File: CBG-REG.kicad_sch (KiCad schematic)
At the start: 36 parts, among them J1 Conn_01x09_Socket, J2 Conn_01x09_Socket, U1 AD8560ACP-REEL7, U2 AD8560ACP-REEL7, U4 74LVC2G04

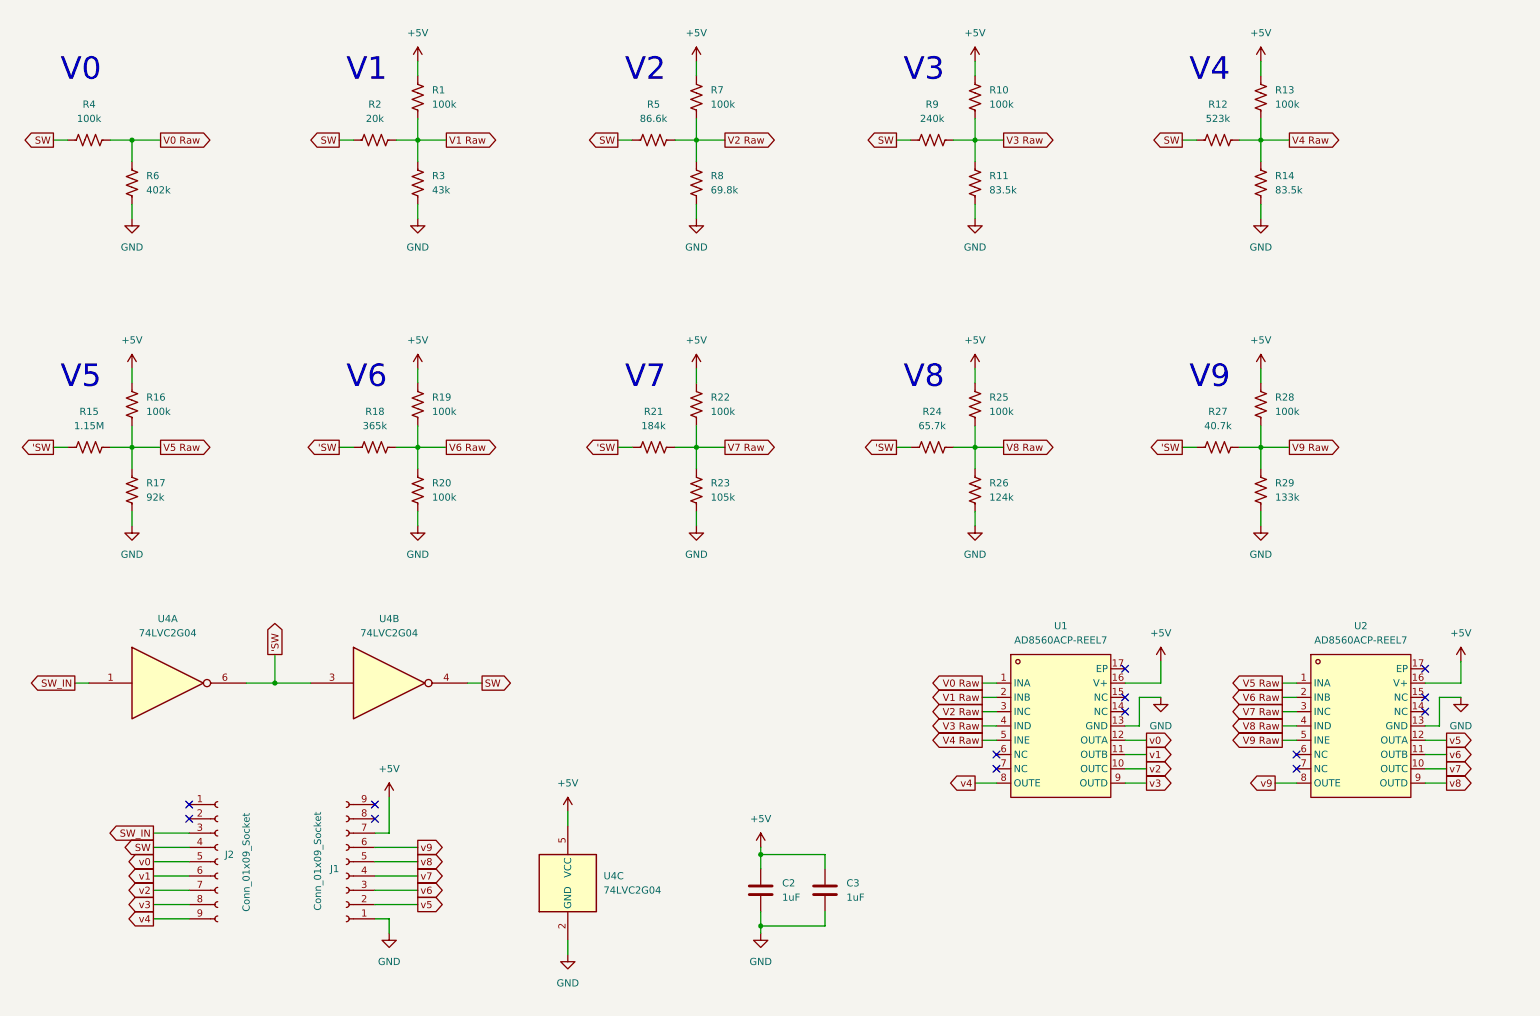
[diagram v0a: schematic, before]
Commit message: fix: Update resistor values to those in stock at JLCPCB
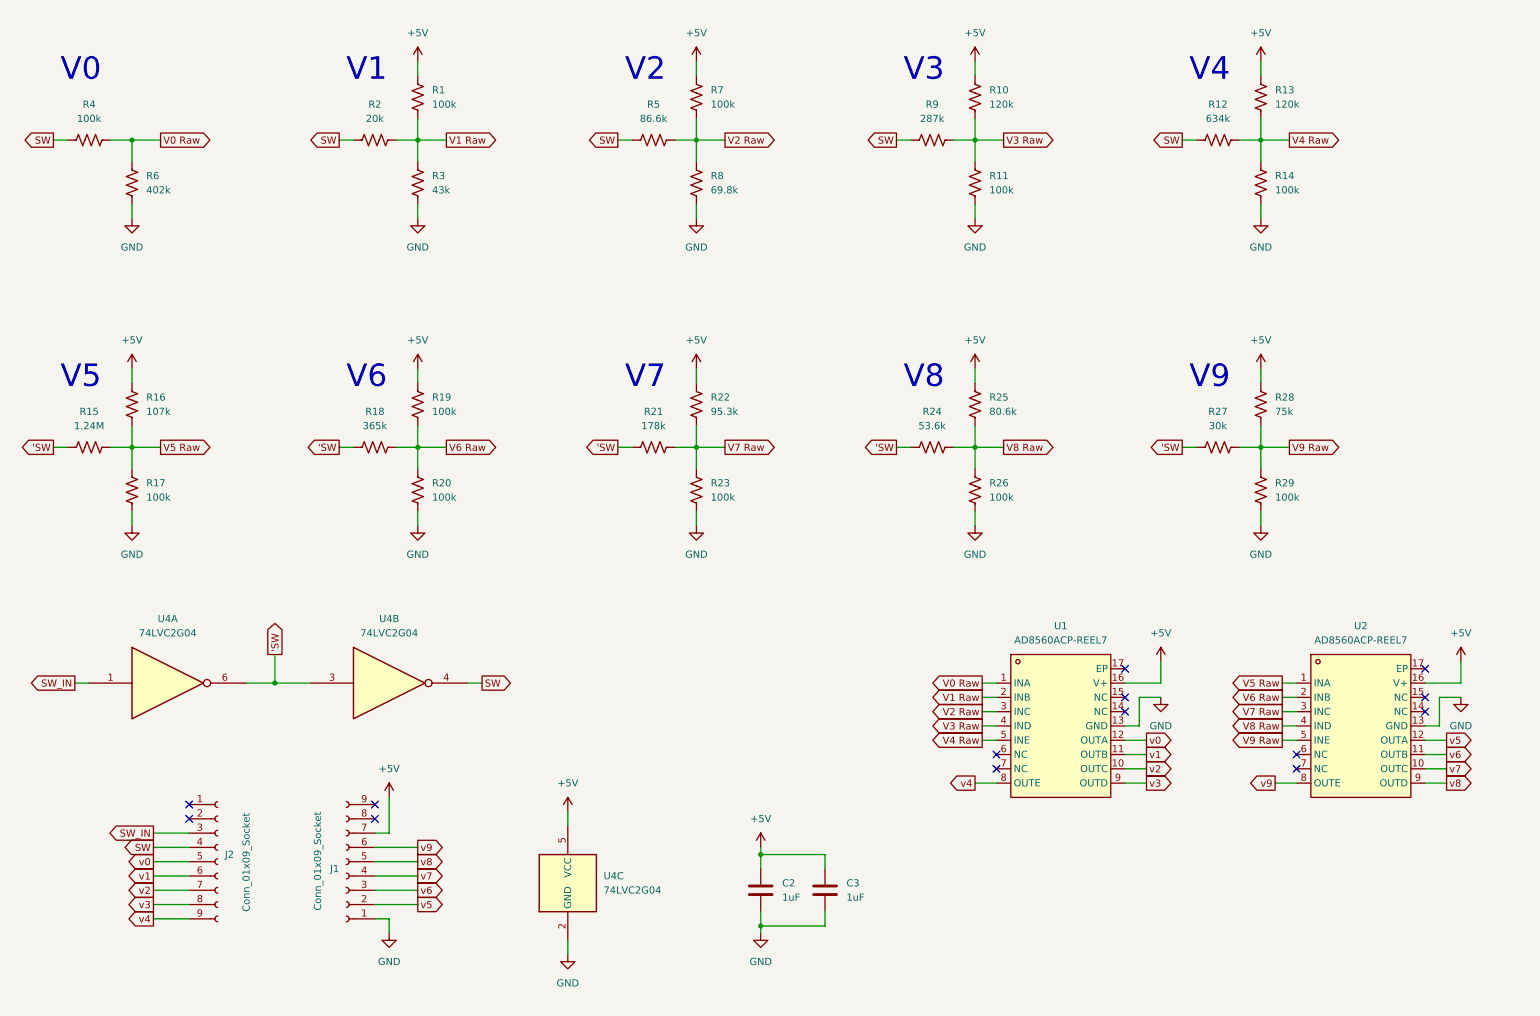
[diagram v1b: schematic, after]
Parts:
- R10, R13: value 100k -> 120k; LCSC C414506 -> C325641
- R11, R14: value 83.5k -> 100k; LCSC C3915798 -> C414506
- R12: value 523k -> 634k; LCSC C5126197 -> C321970
- R15: value 1.15M -> 1.24M; LCSC C2100176 -> C367719
- R16: value 100k -> 107k; LCSC C414506 -> C103221
- R17: value 92k -> 100k; LCSC C4024522 -> C414506
- R21: value 184k -> 178k; LCSC C2505474 -> C103349
- R22: value 100k -> 95.3k; LCSC C414506 -> C912224
- R23: value 105k -> 100k; LCSC C100713 -> C414506
- R24: value 65.7k -> 53.6k; LCSC C2498169 -> C103706
- R25: value 100k -> 80.6k; LCSC C414506 -> C2933260
- R26: value 124k -> 100k; LCSC C2889164 -> C414506
- R27: value 40.7k -> 30k; LCSC C2495443 -> C667692
- R28: value 100k -> 75k; LCSC C414506 -> C881187
- R29: value 133k -> 100k; LCSC C317180 -> C414506
- R9: value 240k -> 287k; LCSC C881412 -> C13174
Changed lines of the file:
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@@
       (effects (font (size 1.27 1.27)) (justify left))
     )
-    (property "Value" "100k" (at 187.96 34.29 0)
+    (property "Value" "120k" (at 187.96 34.29 0)
       (effects (font (size 1.27 1.27)) (justify left))
     )
@@
       (effects (font (size 1.27 1.27)) hide)
     )
-    (property "LCSC" "C414506" (at 185.42 33.02 0)
+    (property "LCSC" "C325641" (at 185.42 33.02 0)
       (effects (font (size 1.27 1.27)) hide)
     )
@@
       (effects (font (size 1.27 1.27)) (justify left))
     )
-    (property "Value" "105k" (at 138.43 104.14 0)
+    (property "Value" "100k" (at 138.43 104.14 0)
       (effects (font (size 1.27 1.27)) (justify left))
     )
@@
       (effects (font (size 1.27 1.27)) hide)
     )
-    (property "LCSC" "C100713" (at 135.89 102.87 0)
+    (property "LCSC" "C414506" (at 135.89 102.87 0)
       (effects (font (size 1.27 1.27)) hide)
     )
@@
       (effects (font (size 1.27 1.27)) (justify left))
     )
-    (property "Value" "100k" (at 238.76 88.9 0)
+    (property "Value" "75k" (at 238.76 88.9 0)
       (effects (font (size 1.27 1.27)) (justify left))
     )
@@
       (effects (font (size 1.27 1.27)) hide)
     )
-    (property "LCSC" "C414506" (at 236.22 87.63 0)
+    (property "LCSC" "C881187" (at 236.22 87.63 0)
       (effects (font (size 1.27 1.27)) hide)
     )
@@
       (effects (font (size 1.27 1.27)) (justify left))
     )
-    (property "Value" "83.5k" (at 238.76 49.53 0)
+    (property "Value" "100k" (at 238.76 49.53 0)
       (effects (font (size 1.27 1.27)) (justify left))
     )
@@
       (effects (font (size 1.27 1.27)) hide)
     )
-    (property "LCSC" "C3915798" (at 236.22 48.26 0)
+    (property "LCSC" "C414506" (at 236.22 48.26 0)
       (effects (font (size 1.27 1.27)) hide)
     )
@@
       (effects (font (size 1.27 1.27)) (justify left))
     )
-    (property "Value" "83.5k" (at 187.96 49.53 0)
+    (property "Value" "100k" (at 187.96 49.53 0)
       (effects (font (size 1.27 1.27)) (justify left))
     )
@@
       (effects (font (size 1.27 1.27)) hide)
     )
-    (property "LCSC" "C3915798" (at 185.42 48.26 0)
+    (property "LCSC" "C414506" (at 185.42 48.26 0)
       (effects (font (size 1.27 1.27)) hide)
     )
@@
       (effects (font (size 1.27 1.27)) (justify left))
     )
-    (property "Value" "100k" (at 138.43 88.9 0)
+    (property "Value" "95.3k" (at 138.43 88.9 0)
       (effects (font (size 1.27 1.27)) (justify left))
     )
@@
       (effects (font (size 1.27 1.27)) hide)
     )
-    (property "LCSC" "C414506" (at 135.89 87.63 0)
+    (property "LCSC" "C912224" (at 135.89 87.63 0)
       (effects (font (size 1.27 1.27)) hide)
     )
@@
       (effects (font (size 1.27 1.27)))
     )
-    (property "Value" "65.7k" (at 177.8 91.44 90)
+    (property "Value" "53.6k" (at 177.8 91.44 90)
       (effects (font (size 1.27 1.27)))
     )
@@
       (effects (font (size 1.27 1.27)) hide)
     )
-    (property "LCSC" "C2498169" (at 177.8 95.25 90)
+    (property "LCSC" "C103706" (at 177.8 95.25 90)
       (effects (font (size 1.27 1.27)) hide)
     )
@@
       (effects (font (size 1.27 1.27)) (justify left))
     )
-    (property "Value" "133k" (at 238.76 104.14 0)
+    (property "Value" "100k" (at 238.76 104.14 0)
       (effects (font (size 1.27 1.27)) (justify left))
     )
@@
       (effects (font (size 1.27 1.27)) hide)
     )
-    (property "LCSC" "C317180" (at 236.22 102.87 0)
+    (property "LCSC" "C414506" (at 236.22 102.87 0)
       (effects (font (size 1.27 1.27)) hide)
     )
@@
       (effects (font (size 1.27 1.27)))
     )
-    (property "Value" "1.15M" (at 27.94 91.44 90)
+    (property "Value" "1.24M" (at 27.94 91.44 90)
       (effects (font (size 1.27 1.27)))
     )
@@
       (effects (font (size 1.27 1.27)) hide)
     )
-    (property "LCSC" "C2100176" (at 27.94 95.25 90)
+    (property "LCSC" "C367719" (at 27.94 95.25 90)
       (effects (font (size 1.27 1.27)) hide)
     )
@@
       (effects (font (size 1.27 1.27)) (justify left))
     )
-    (property "Value" "100k" (at 187.96 88.9 0)
+    (property "Value" "80.6k" (at 187.96 88.9 0)
       (effects (font (size 1.27 1.27)) (justify left))
     )
@@
       (effects (font (size 1.27 1.27)) hide)
     )
-    (property "LCSC" "C414506" (at 185.42 87.63 0)
+    (property "LCSC" "C2933260" (at 185.42 87.63 0)
       (effects (font (size 1.27 1.27)) hide)
     )
@@
       (effects (font (size 1.27 1.27)))
     )
-    (property "Value" "184k" (at 128.27 91.44 90)
+    (property "Value" "178k" (at 128.27 91.44 90)
       (effects (font (size 1.27 1.27)))
     )
@@
       (effects (font (size 1.27 1.27)) hide)
     )
-    (property "LCSC" "C2505474" (at 128.27 95.25 90)
+    (property "LCSC" "C103349" (at 128.27 95.25 90)
       (effects (font (size 1.27 1.27)) hide)
     )
@@
       (effects (font (size 1.27 1.27)))
     )
-    (property "Value" "523k" (at 228.6 36.83 90)
+    (property "Value" "634k" (at 228.6 36.83 90)
       (effects (font (size 1.27 1.27)))
     )
@@
       (effects (font (size 1.27 1.27)) hide)
     )
-    (property "LCSC" "C5126197" (at 228.6 40.64 90)
+    (property "LCSC" "C321970" (at 228.6 40.64 90)
       (effects (font (size 1.27 1.27)) hide)
     )
@@
       (effects (font (size 1.27 1.27)) (justify left))
     )
-    (property "Value" "124k" (at 187.96 104.14 0)
+    (property "Value" "100k" (at 187.96 104.14 0)
       (effects (font (size 1.27 1.27)) (justify left))
     )
@@
       (effects (font (size 1.27 1.27)) hide)
     )
-    (property "LCSC" "C2889164" (at 185.42 102.87 0)
+    (property "LCSC" "C414506" (at 185.42 102.87 0)
       (effects (font (size 1.27 1.27)) hide)
     )
@@
       (effects (font (size 1.27 1.27)))
     )
-    (property "Value" "40.7k" (at 228.6 91.44 90)
+    (property "Value" "30k" (at 228.6 91.44 90)
       (effects (font (size 1.27 1.27)))
     )
@@
       (effects (font (size 1.27 1.27)) hide)
     )
-    (property "LCSC" "C2495443" (at 228.6 95.25 90)
+    (property "LCSC" "C667692" (at 228.6 95.25 90)
       (effects (font (size 1.27 1.27)) hide)
     )
@@
       (effects (font (size 1.27 1.27)) (justify left))
     )
-    (property "Value" "92k" (at 38.1 104.14 0)
+    (property "Value" "100k" (at 38.1 104.14 0)
       (effects (font (size 1.27 1.27)) (justify left))
     )
@@
       (effects (font (size 1.27 1.27)) hide)
     )
-    (property "LCSC" "C4024522" (at 35.56 102.87 0)
+    (property "LCSC" "C414506" (at 35.56 102.87 0)
       (effects (font (size 1.27 1.27)) hide)
     )
@@
       (effects (font (size 1.27 1.27)) (justify left))
     )
-    (property "Value" "100k" (at 38.1 88.9 0)
+    (property "Value" "107k" (at 38.1 88.9 0)
       (effects (font (size 1.27 1.27)) (justify left))
     )
@@
       (effects (font (size 1.27 1.27)) hide)
     )
-    (property "LCSC" "C414506" (at 35.56 87.63 0)
+    (property "LCSC" "C103221" (at 35.56 87.63 0)
       (effects (font (size 1.27 1.27)) hide)
     )
@@
       (effects (font (size 1.27 1.27)) (justify left))
     )
-    (property "Value" "100k" (at 238.76 34.29 0)
+    (property "Value" "120k" (at 238.76 34.29 0)
       (effects (font (size 1.27 1.27)) (justify left))
     )
@@
       (effects (font (size 1.27 1.27)) hide)
     )
-    (property "LCSC" "C414506" (at 236.22 33.02 0)
+    (property "LCSC" "C325641" (at 236.22 33.02 0)
       (effects (font (size 1.27 1.27)) hide)
     )
@@
       (effects (font (size 1.27 1.27)))
     )
-    (property "Value" "240k" (at 177.8 36.83 90)
+    (property "Value" "287k" (at 177.8 36.83 90)
       (effects (font (size 1.27 1.27)))
     )
@@
       (effects (font (size 1.27 1.27)) hide)
     )
-    (property "LCSC" "C881412" (at 177.8 40.64 90)
-      (effects (font (size 1.27 1.27)) hide)
-    )
+    (property "LCSC" "C13174" (at 177.8 40.64 90)
+      (effects (font (size 1.27 1.27)) hide)
+    )

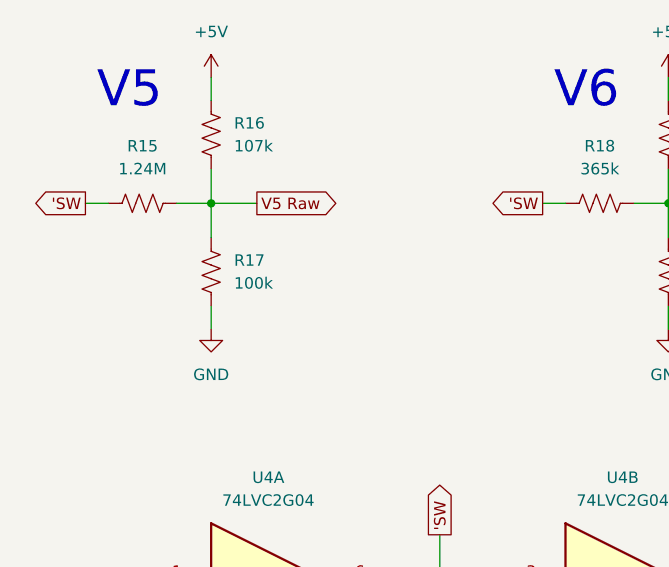
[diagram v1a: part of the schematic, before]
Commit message: feat: Update accuracy of V5 signal
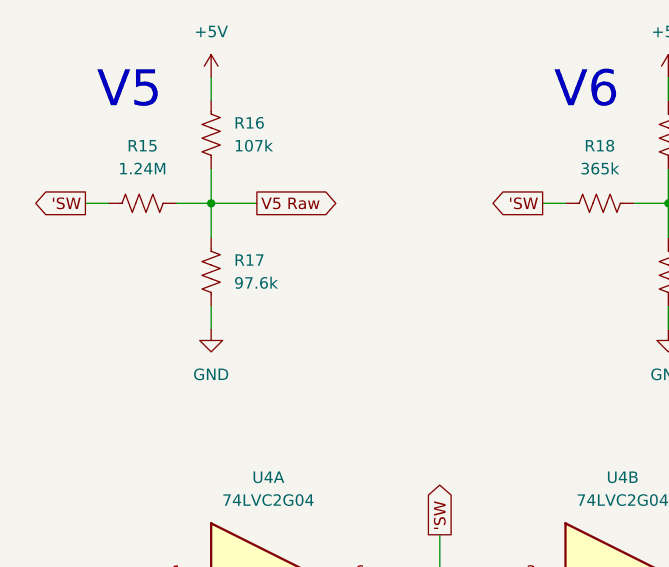
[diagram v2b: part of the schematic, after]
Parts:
- R17: value 100k -> 97.6k; LCSC C414506 -> C507495
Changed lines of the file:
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@@
       (effects (font (size 1.27 1.27)) (justify left))
     )
-    (property "Value" "100k" (at 38.1 104.14 0)
+    (property "Value" "97.6k" (at 38.1 104.14 0)
       (effects (font (size 1.27 1.27)) (justify left))
     )
@@
       (effects (font (size 1.27 1.27)) hide)
     )
-    (property "LCSC" "C414506" (at 35.56 102.87 0)
+    (property "LCSC" "C507495" (at 35.56 102.87 0)
       (effects (font (size 1.27 1.27)) hide)
     )
